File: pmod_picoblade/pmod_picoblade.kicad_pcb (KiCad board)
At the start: 2 copper layers, 40 x 24 mm, 7 parts, among them J1 SALEAE_0-3, J2 SALEAE_0-3, J3 SPI, J4 PMOD, J5 SALEAE_4-7, J6 SALEAE_4-7, J7 UART

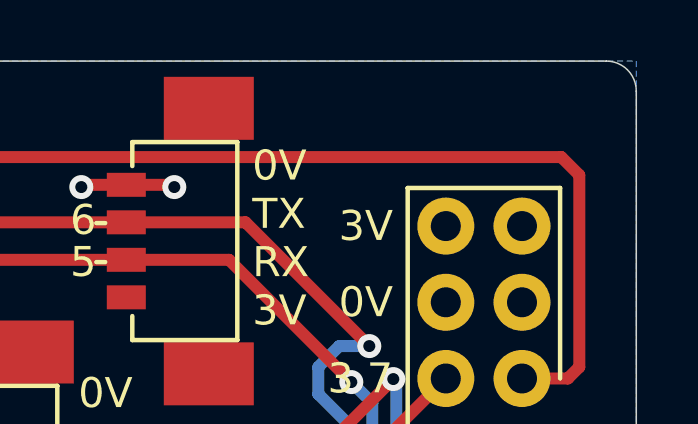
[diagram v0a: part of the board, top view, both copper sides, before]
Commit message: Update with silk date/rev code
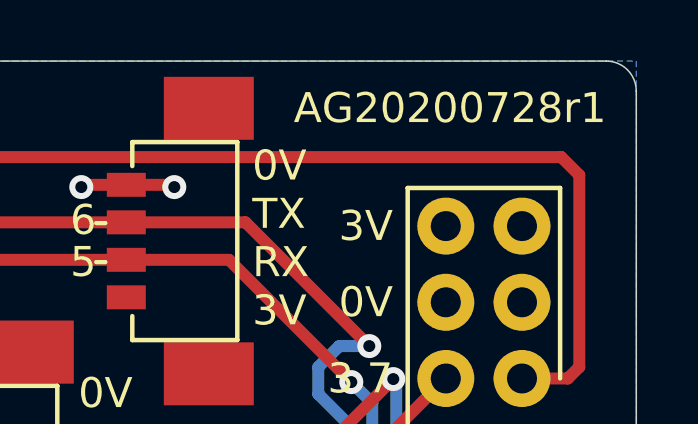
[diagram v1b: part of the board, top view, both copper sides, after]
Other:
- board text added: "AG20200728r1"
